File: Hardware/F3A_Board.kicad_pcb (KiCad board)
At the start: 2 copper layers, 90.2 x 71.1 mm, 13 parts, among them J1 Conn_01x03, U1 LD1117AV33, U2 W25Q64V

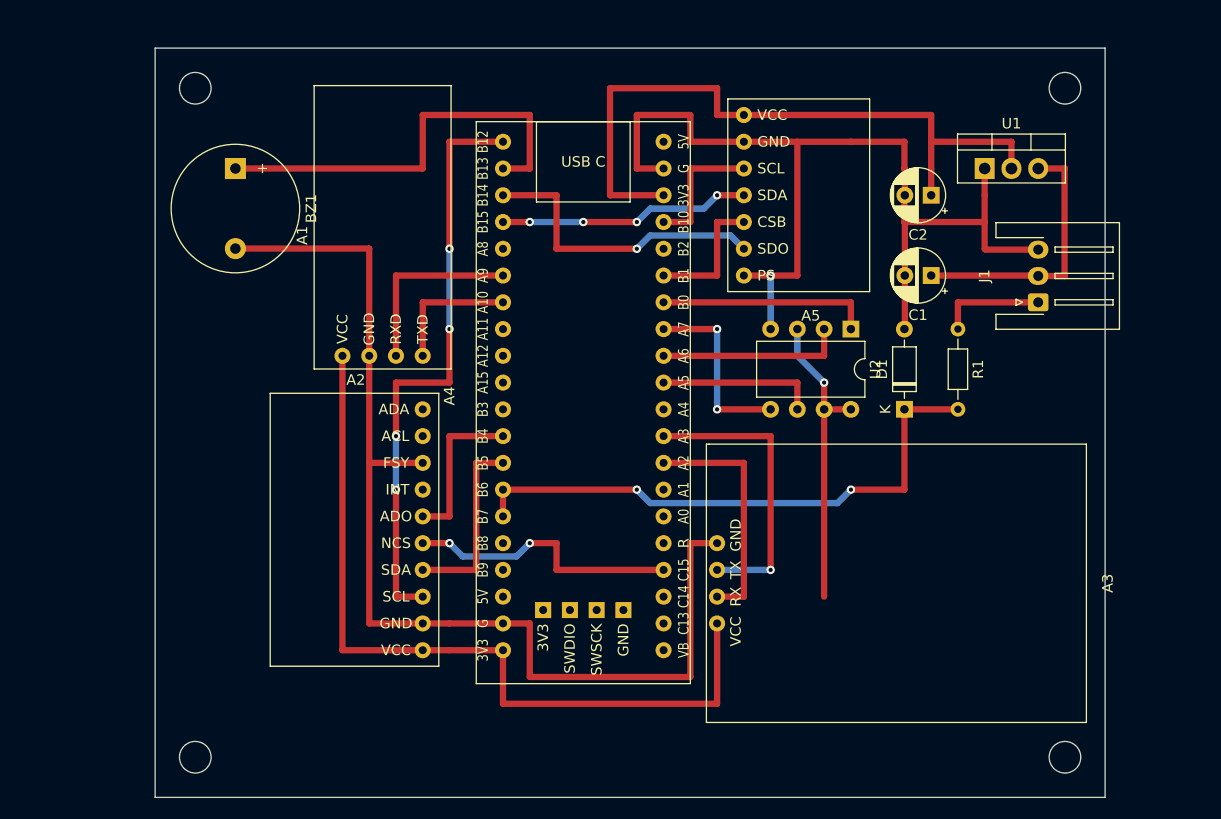
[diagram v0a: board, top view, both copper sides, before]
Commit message: Adding Zener datasheets
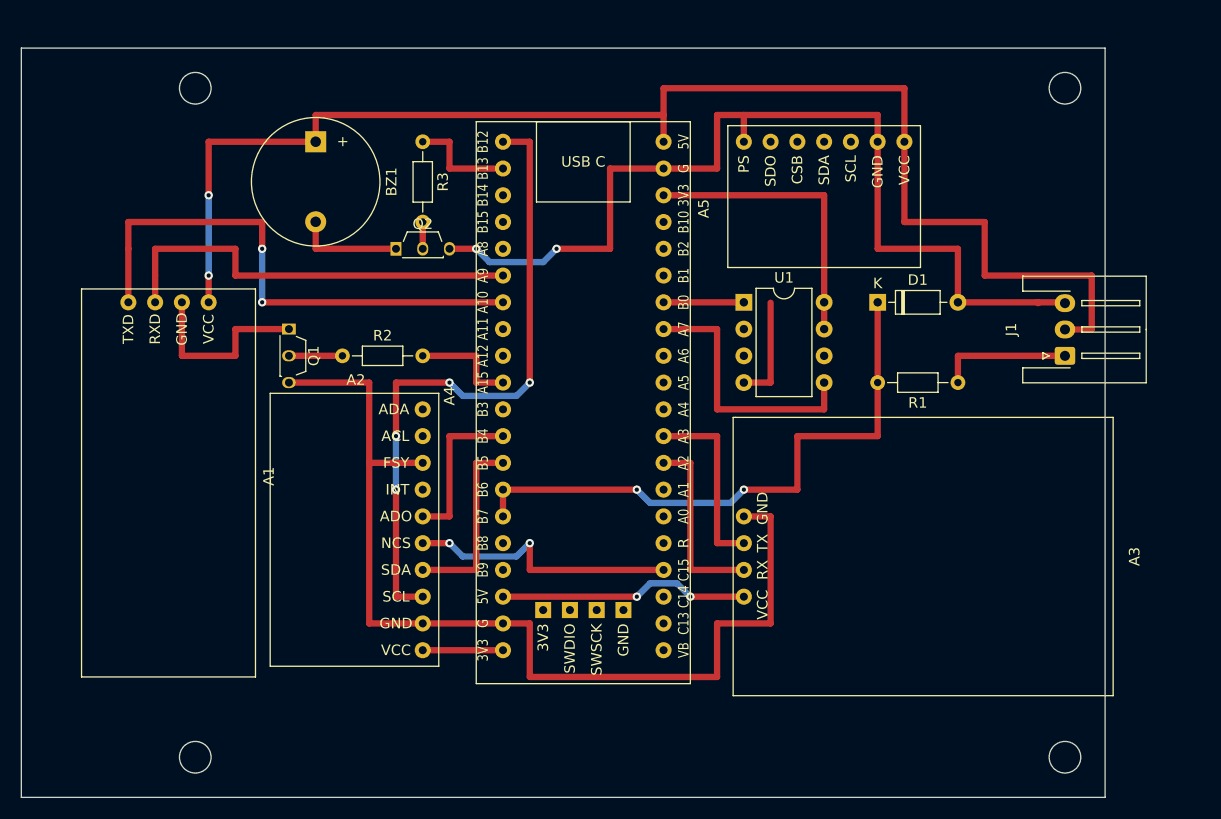
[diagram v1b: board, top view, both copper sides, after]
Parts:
- removed C1: 100nF, Capacitor_THT:CP_Radial_D5.0mm_P2.50mm
- removed C2: 10uF, Capacitor_THT:CP_Radial_D5.0mm_P2.50mm
- removed the U1 at (205.7, 83.8)
- added Q1: BC550, Package_TO_SOT_THT:TO-92S_Wide, F.Cu at (139.7, 99.1)
- added Q2: BC550, Package_TO_SOT_THT:TO-92S_Wide, F.Cu at (149.9, 91.4)
- added R2: 510, Resistor_THT:R_Axial_DIN0204_L3.6mm_D1.6mm_P7.62mm_Horizontal, F.Cu at (144.8, 101.6)
- added R3: 1K, Resistor_THT:R_Axial_DIN0204_L3.6mm_D1.6mm_P7.62mm_Horizontal, F.Cu at (152.4, 81.3)
- A1: value HC08 -> DSD_TECH_HC06; footprint F3A_Modules:HC08 -> F3A_Modules:DSD_TECH_HC06
- R1: value 1k -> 510
- moved A1 30.6 mm to (128.3, 113.0), turned to 90 degrees
- moved D1 10.5 mm to (195.6, 96.5), turned to 0 degrees
- moved U1 10.5 mm to (182.9, 96.5), turned to 0 degrees
- moved BZ1 8.03 mm to (142.2, 81.3)
- moved J1 5.68 mm to (213.4, 101.6)
- moved R1 5.08 mm to (203.2, 104.1), turned to 180 degrees
- moved A3 3.59 mm to (200.7, 120.7)
- moved A5 1.80 mm to (190.5, 87.6), turned to 270 degrees
- renumbered U2 to U1
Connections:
- A1 pad 27: +3V3 -> +5V
- A1 pad 28: GND -> Net-(A1-Pad28)
- A2 pad 10: Net-(A2-Pad10) -> (no net)
- A2 pad 7: Net-(A2-Pad7) -> (no net)
- A2 pad 9: Net-(A2-Pad9) -> (no net)
- A3 pad 1: +3V3 -> +5V
- A4 pad 10: Net-(A4-Pad10) -> HC06_PWR_CTRL
- A4 pad 11: Net-(A4-Pad11) -> (no net)
- A4 pad 16: Net-(A4-Pad16) -> (no net)
- A4 pad 17: Net-(A4-Pad17) -> (no net)
- A4 pad 18: Net-(A4-Pad18) -> +5V
- A4 pad 2: Net-(A4-Pad2) -> Buzzer_PWR
- A4 pad 21: Net-(A4-Pad21) -> +5V
- A4 pad 25: Net-(A4-Pad25) -> (no net)
- A4 pad 31: Net-(A4-Pad31) -> (no net)
- A4 pad 34: Net-(A4-Pad34) -> (no net)
- A4 pad 35: Net-(A4-Pad35) -> (no net)
- A4 pad 36: Net-(A4-Pad36) -> (no net)
- A4 pad 38: Net-(A4-Pad38) -> (no net)
- A4 pad 39: Net-(A4-Pad39) -> (no net)
- A4 pad 40: Net-(A4-Pad40) -> (no net)
- A4 pad 5: Net-(A4-Pad5) -> (no net)
- A4 pad 8: Net-(A4-Pad8) -> (no net)
- A4 pad 9: Net-(A4-Pad9) -> (no net)
- A5 pad 1: +3V3 -> +5V
- BZ1 pad 1: Net-(A4-Pad2) -> +5V
- BZ1 pad 2: GND -> Net-(BZ1-Pad2)
- J1 pad 2: +7.5V -> +5V
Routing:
- net +5V: track 0.00 -> 156.1 mm, vias 0 -> 4
- net +3V3: track 171.2 -> 35.6 mm, vias 1 -> 0
- net Net-(A4-Pad2): track 40.6 -> 0.00 mm
- net /UART1_RX: track 12.7 -> 50.8 mm, vias 0 -> 2
- net /SPI2_SDO: track 29.0 -> 0.00 mm, vias 1 -> 0
- net +7.5V: track 25.5 -> 0.00 mm
- net /SPI2_SDI: track 23.9 -> 0.00 mm, vias 4 -> 0
- net /UART1_TX: track 17.8 -> 40.6 mm
- net /SPI1_SDO: track 17.8 -> 0.00 mm
- net Net-(A1-Pad28): track 0.00 -> 17.8 mm
- net /SPI1_SCL: track 15.2 -> 0.00 mm
- net /SPI2_SCL: track 12.7 -> 0.00 mm
- net /SPI2_CS: track 12.7 -> 0.00 mm
- net /SPI1_CS: track 20.3 -> 7.62 mm
- net Net-(BZ1-Pad2): track 0.00 -> 10.2 mm
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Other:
- board size 90.2 x 71.1 mm -> 102.9 x 71.1 mm

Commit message: PCBnew updated Created step file
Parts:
- moved U1 15.5 mm to (198.1, 94.0), turned to 270 degrees
- moved R1 11.4 mm to (208.3, 94.0), turned to 270 degrees
- moved D1 9.16 mm to (203.2, 101.6), turned to 90 degrees
- moved A5 8.98 mm to (196.8, 81.3), turned to 0 degrees
- moved A4 7.18 mm to (172.7, 100.3)
- moved Q1 7.18 mm to (144.8, 94.0)
- moved R2 7.18 mm to (149.9, 96.5)
- moved A1 7.18 mm to (133.3, 108.0)
- moved A2 7.18 mm to (151.1, 113.0)
- moved BZ1 7.18 mm to (147.3, 76.2)
- moved Q2 7.18 mm to (154.9, 86.4)
- moved R3 7.18 mm to (157.5, 76.2)
- moved A3 5.68 mm to (205.7, 118.1)
- moved J1 5.68 mm to (218.4, 99.1)
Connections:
- net Buzzer_PWR renamed Buzzer_PWR_CTRL
- A4 pad 14: PWM_IN -> RC_PWM
- A4 pad 15: PWM_IN -> (no net)
- D1 pad 1: PWM_IN -> RC_PWM
- R1 pad 2: PWM_IN -> RC_PWM
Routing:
- net RC_PWM: track 0.00 -> 56.9 mm, vias 0 -> 2
- net PWM_IN: track 56.9 -> 0.00 mm, vias 2 -> 0
- net +3V3: track 35.6 -> 87.4 mm
- net /SPI2_SDO: track 0.00 -> 31.6 mm, vias 0 -> 3
- net /SPI2_SDI: track 0.00 -> 29.0 mm, vias 0 -> 3
- net /SPI1_SDO: track 0.00 -> 17.8 mm
- net /SPI2_CS: track 0.00 -> 15.2 mm
- net /SPI2_SCL: track 0.00 -> 15.2 mm
- net /SPI1_SCL: track 0.00 -> 15.2 mm
- net /SPI1_CS: track 7.62 -> 20.3 mm, vias 0 -> 2
- net +5V: track 156.1 -> 165.1 mm, vias 4 -> 2
- net GND: track 199.3 -> 191.6 mm
- net /SPI1_SDI: track 25.4 -> 17.8 mm, vias 0 -> 2
- net /UART2_RX: track 17.8 -> 20.3 mm
- net /UART2_TX: track 17.8 -> 20.3 mm
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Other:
- board size 102.9 x 71.1 mm -> 101.6 x 68.6 mm
